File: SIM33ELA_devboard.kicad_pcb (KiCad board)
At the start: 4 copper layers, 40 x 24.9 mm, 11 parts, among them J2 Conn_01x13_Pin, U2 SIM33ELA

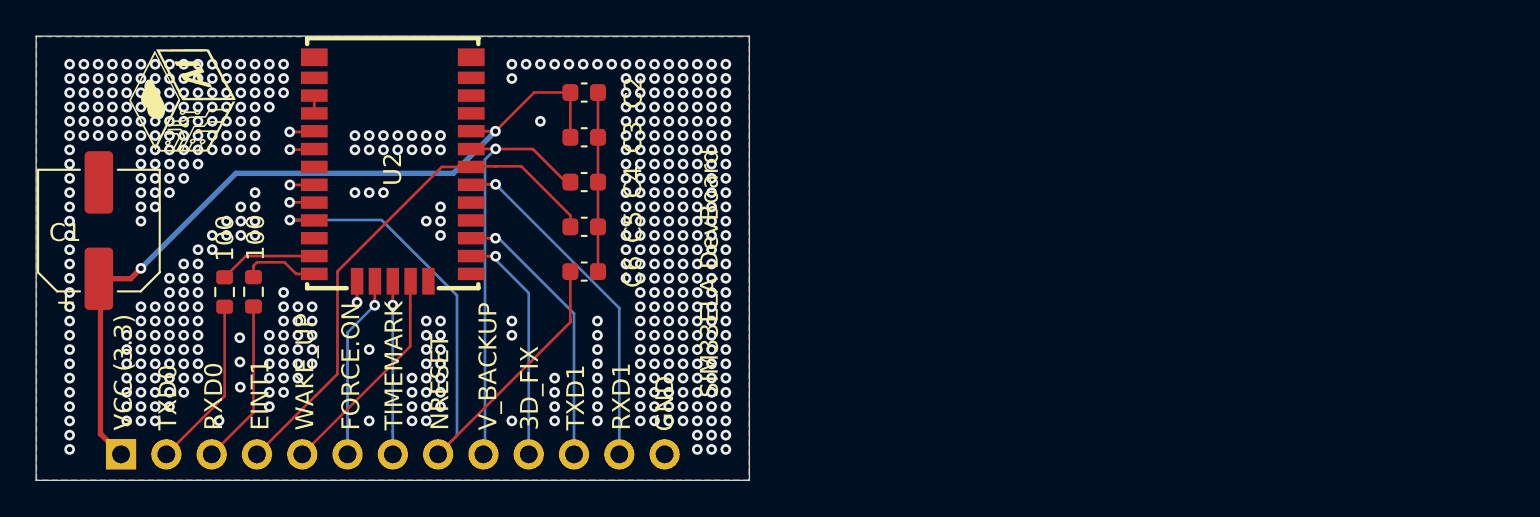
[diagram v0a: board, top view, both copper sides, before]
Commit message: RF modificado, agregado led de POWER
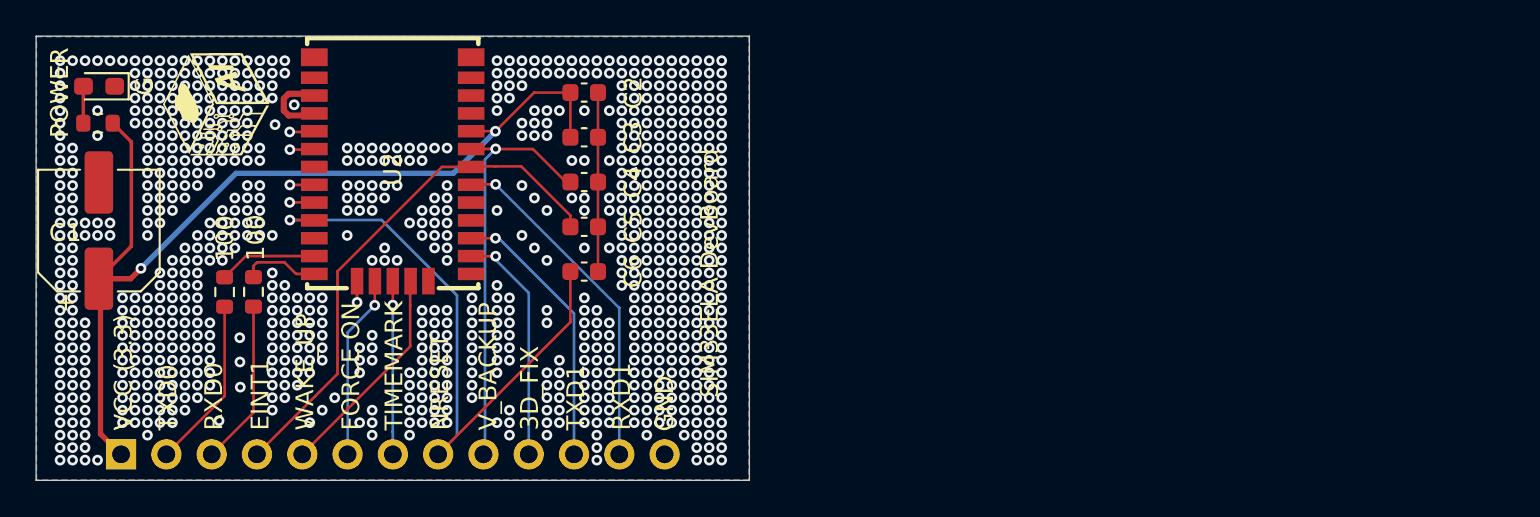
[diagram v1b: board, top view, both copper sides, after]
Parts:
- added POWER: LED_Small, LED_SMD:LED_0603_1608Metric_Pad1.05x0.95mm_HandSolder, F.Cu at (128.3, 83.7)
- added R3: 2.7k, Resistor_SMD:R_0603_1608Metric, F.Cu at (128.2, 85.7)
- moved G*** 1.90 mm to (135.0, 84.7)
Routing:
- net /VCC: track 45.0 -> 54.9 mm
- net Net-(U2-ANT): track 1.00 -> 4.40 mm
- net Net-(D1-A): track 0.00 -> 2.07 mm
- net GND: vias 508 -> 875
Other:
- board text added: "G"

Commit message: por si acaso
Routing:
- net GND: vias 875 -> 876
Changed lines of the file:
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@@
+	)
+	(via
+		(at 137.99 85.11)
+		(size 0.6)
+		(drill 0.3)
+		(layers "F.Cu" "B.Cu")
+		(free yes)
+		(net 18)
 	)
 	(via

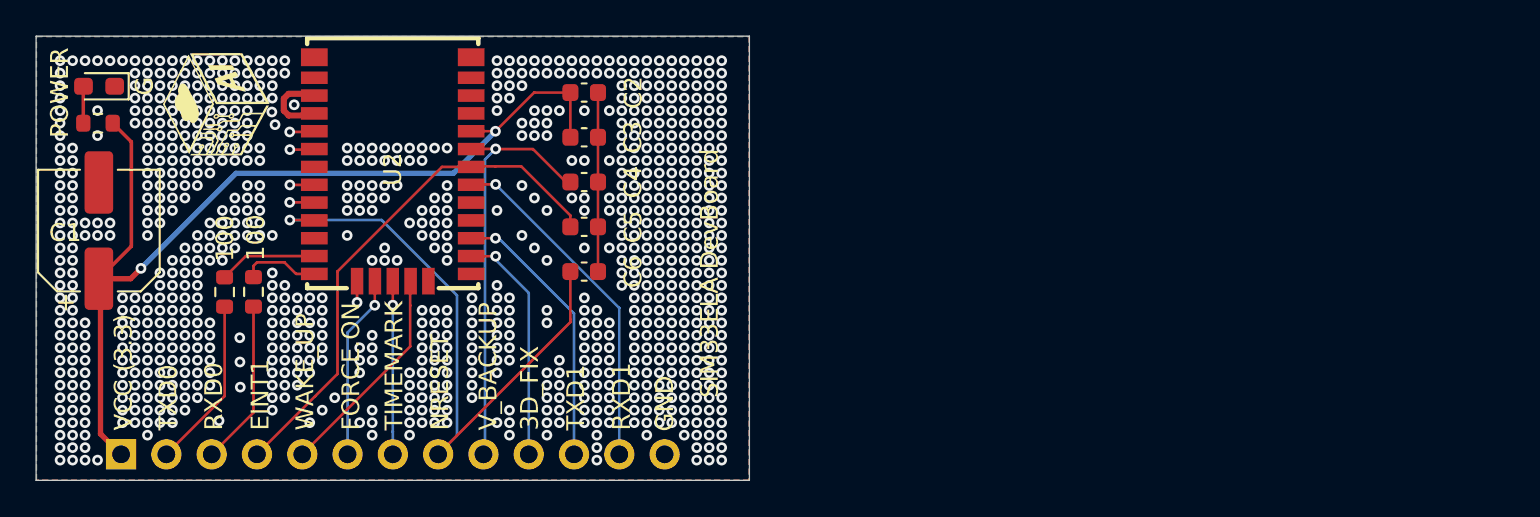
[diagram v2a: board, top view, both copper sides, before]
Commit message: cambio de stack JLCPCB, 2 versiones para microstrip
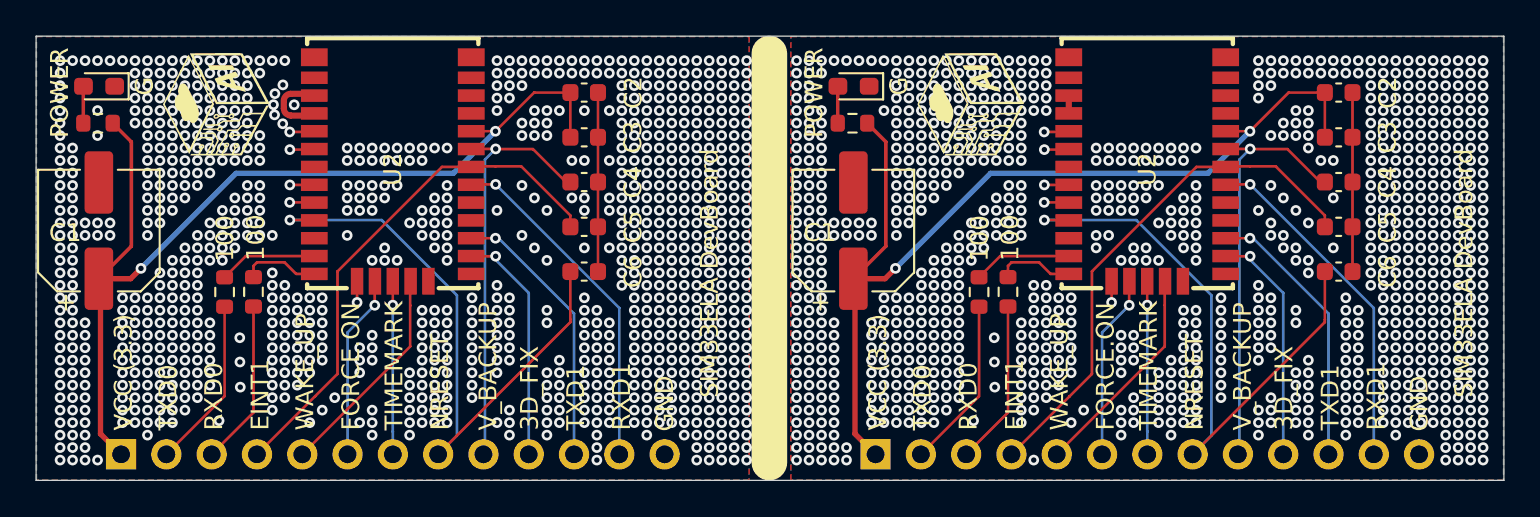
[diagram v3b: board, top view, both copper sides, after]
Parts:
- added C1: 470uF, Capacitor_SMD:CP_Elec_6.3x7.7, F.Cu at (170.6, 91.8)
- added C2: 4.7uF, Capacitor_SMD:C_0603_1608Metric, F.Cu at (197.8, 84.0)
- added C3: 100nF, Capacitor_SMD:C_0603_1608Metric, F.Cu at (197.8, 86.5)
- added C4: 4.7uF, Capacitor_SMD:C_0603_1608Metric, F.Cu at (197.8, 89.0)
- added C5: 15pF, Capacitor_SMD:C_0603_1608Metric, F.Cu at (197.8, 91.5)
- added C6: 15pF, Capacitor_SMD:C_0603_1608Metric, F.Cu at (197.8, 94.1)
- added G***: LOGO, Images:LOGOv3.4, F.Cu at (177.3, 84.7)
- added J2: Conn_01x13_Pin, Connector_PinHeader_2.54mm:PinHeader_1x13_P2.54mm_Vertical, B.Cu at (171.8, 104.3)
- added POWER: LED_Small, LED_SMD:LED_0603_1608Metric_Pad1.05x0.95mm_HandSolder, F.Cu at (170.6, 83.7)
- added R1: 100, Resistor_SMD:R_0603_1608Metric, F.Cu at (179.3, 95.2)
- added R2: 100, Resistor_SMD:R_0603_1608Metric, F.Cu at (177.7, 95.2)
- added R3: 2.7k, Resistor_SMD:R_0603_1608Metric, F.Cu at (170.6, 85.7)
- added U2: SIM33ELA, EasyEDA:SIM33ELA, F.Cu at (187.1, 88.3)
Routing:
- net /VCC: track 54.9 -> 109.7 mm, vias 2 -> 4
- net /NRESET: track 35.2 -> 70.3 mm, vias 1 -> 2
- net /EINT1: track 29.4 -> 58.8 mm
- net /V_BAKCUP: track 23.7 -> 47.5 mm, vias 1 -> 2
- net /RXD1: track 19.4 -> 38.7 mm, vias 1 -> 2
- net GND: track 16.7 -> 33.3 mm, vias 876 -> 1886
- net /TXD1: track 15.4 -> 30.8 mm, vias 1 -> 2
- net /3D-FIX: track 13.2 -> 26.5 mm, vias 1 -> 2
- net /WAKE_UP: track 12.2 -> 24.5 mm
- net /FORCE_ON: track 10.4 -> 20.7 mm, vias 1 -> 2
- net /TIMEMARK: track 9.73 -> 19.5 mm, vias 1 -> 2
- net /TXD0: track 9.63 -> 19.3 mm
- net /RXD0: track 9.26 -> 18.5 mm
- net Net-(U2-TXD0): track 5.52 -> 11.0 mm
- net Net-(U2-RXD0): track 4.39 -> 8.78 mm
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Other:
- board size 40 x 24.9 mm -> 82.3 x 24.9 mm
- board text added: "curvo"
- board text added: "recto"

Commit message: cambios finales
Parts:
- R3: value 2.7k -> 4.7k
- renumbered POWER to D1
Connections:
- U2 pad 16: Net-(U2-ANT) -> /RF_SIGNAL1
- U2 pad 17: Net-(U2-ANT) -> /RF_SIGNAL1
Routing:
- net GND: track 33.3 -> 22.5 mm, vias 1886 -> 1201
- net /RF_SIGNAL1: track 0.00 -> 4.14 mm
- net Net-(U2-ANT): track 6.56 -> 4.02 mm
- added copper zone on F.Cu, net /RF_SIGNAL1

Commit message: diseño final
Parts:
- removed the C1 at (170.6, 91.8)
- removed the C2 at (197.8, 84.0)
- removed the C3 at (197.8, 86.5)
- removed the C4 at (197.8, 89.0)
- removed the C5 at (197.8, 91.5)
- removed the C6 at (197.8, 94.1)
- removed G*** (x2): LOGO, Images:LOGOv3.4
- removed the J2 at (171.8, 104.3)
- removed POWER: LED_Small, LED_SMD:LED_0603_1608Metric_Pad1.05x0.95mm_HandSolder
- removed the R1 at (179.3, 95.2)
- removed the R2 at (177.7, 95.2)
- removed the R3 at (170.6, 85.7)
- removed the U2 at (187.1, 88.3)
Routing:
- net /VCC: track 109.7 -> 54.9 mm, vias 4 -> 2
- net /NRESET: track 70.3 -> 35.2 mm, vias 2 -> 1
- net /EINT1: track 58.8 -> 29.4 mm
- net /V_BAKCUP: track 47.5 -> 23.7 mm, vias 2 -> 1
- net /RXD1: track 38.7 -> 19.4 mm, vias 2 -> 1
- net /TXD1: track 30.8 -> 15.4 mm, vias 2 -> 1
- net /3D-FIX: track 26.5 -> 13.2 mm, vias 2 -> 1
- net /WAKE_UP: track 24.5 -> 12.2 mm
- net GND: track 22.5 -> 11.2 mm, vias 1201 -> 581
- net /FORCE_ON: track 20.7 -> 10.4 mm, vias 2 -> 1
- net /TIMEMARK: track 19.5 -> 9.73 mm, vias 2 -> 1
- net /TXD0: track 19.3 -> 9.63 mm
- net /RXD0: track 18.5 -> 9.26 mm
- net Net-(U2-TXD0): track 11.0 -> 5.52 mm
- net Net-(U2-RXD0): track 8.78 -> 4.39 mm
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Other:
- board size 82.3 x 24.9 mm -> 39.4 x 24.9 mm
- board text removed: "recto"

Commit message: aaa
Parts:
- removed C1: 470uF, Capacitor_SMD:CP_Elec_6.3x7.7
- removed J2: Conn_01x13_Pin, Connector_PinHeader_2.54mm:PinHeader_1x13_P2.54mm_Vertical
- added J1: Conn_01x14_Pin, Connector_PinHeader_2.54mm:PinHeader_1x14_P2.54mm_Vertical, B.Cu at (128.0, 104.3)
- added JP1: SolderJumper_2_Open, Jumper:SolderJumper-2_P1.3mm_Open_RoundedPad1.0x1.5mm, F.Cu at (128.2, 91.3)
- added U1: XC6206P332MR, EasyEDA:SOT-23-3_L2.9-W1.6-P1.90-LS2.8-BR, F.Cu at (127.2, 98.4)
- added kibuzzard-6A1C62F4: G***, kibuzzard-6A1C62F4, F.Cu at (162.3, 90.8)
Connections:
- R3 pad 2: /VCC -> Net-(JP1-A)
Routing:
- net /V_BAKCUP: track 23.7 -> 7.17 mm
- net Net-(JP1-A): track 0.00 -> 6.16 mm
- net /LDO: track 0.00 -> 6.13 mm
- net /VCC: track 54.9 -> 56.9 mm
- net /NRESET: track 35.2 -> 34.3 mm
- net GND: vias 581 -> 420
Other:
- board text added: "LDO"
- board text removed: "GND"
- board text removed: "SIM33ELA DevBoard"
